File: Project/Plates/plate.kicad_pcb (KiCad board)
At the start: 2 copper layers, 242.9 x 88.2 mm, 45 parts

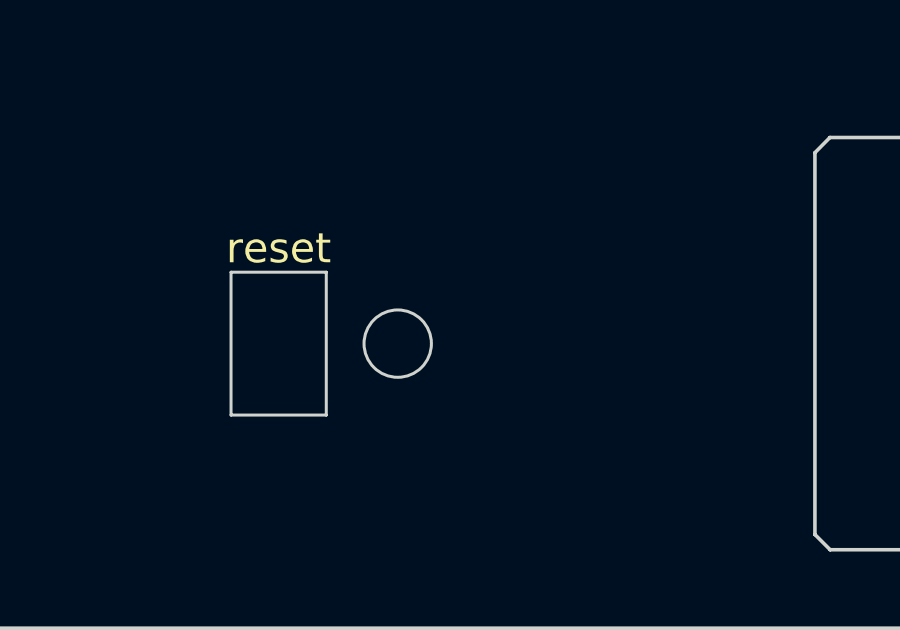
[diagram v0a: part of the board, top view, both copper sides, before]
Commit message: pcb & plate revision
move mux, add cutout for all plates for boot
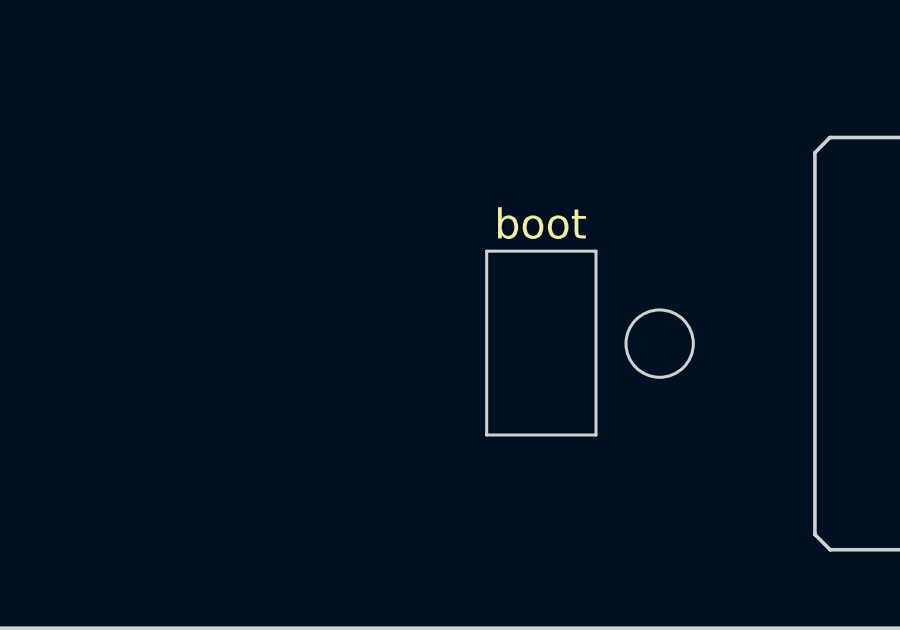
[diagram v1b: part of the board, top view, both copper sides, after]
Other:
- outline, holes or cut-outs redrawn
- board text added: "boot"
- board text removed: "reset"
